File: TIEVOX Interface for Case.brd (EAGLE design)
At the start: 67.5 x 70 mm, 27 parts, among them IC1 DMMT5401, IC2 DMMT5401, U1 DMP2305U-7, U2 DMP2305U-7, U4 CAT24C32.UDFN8

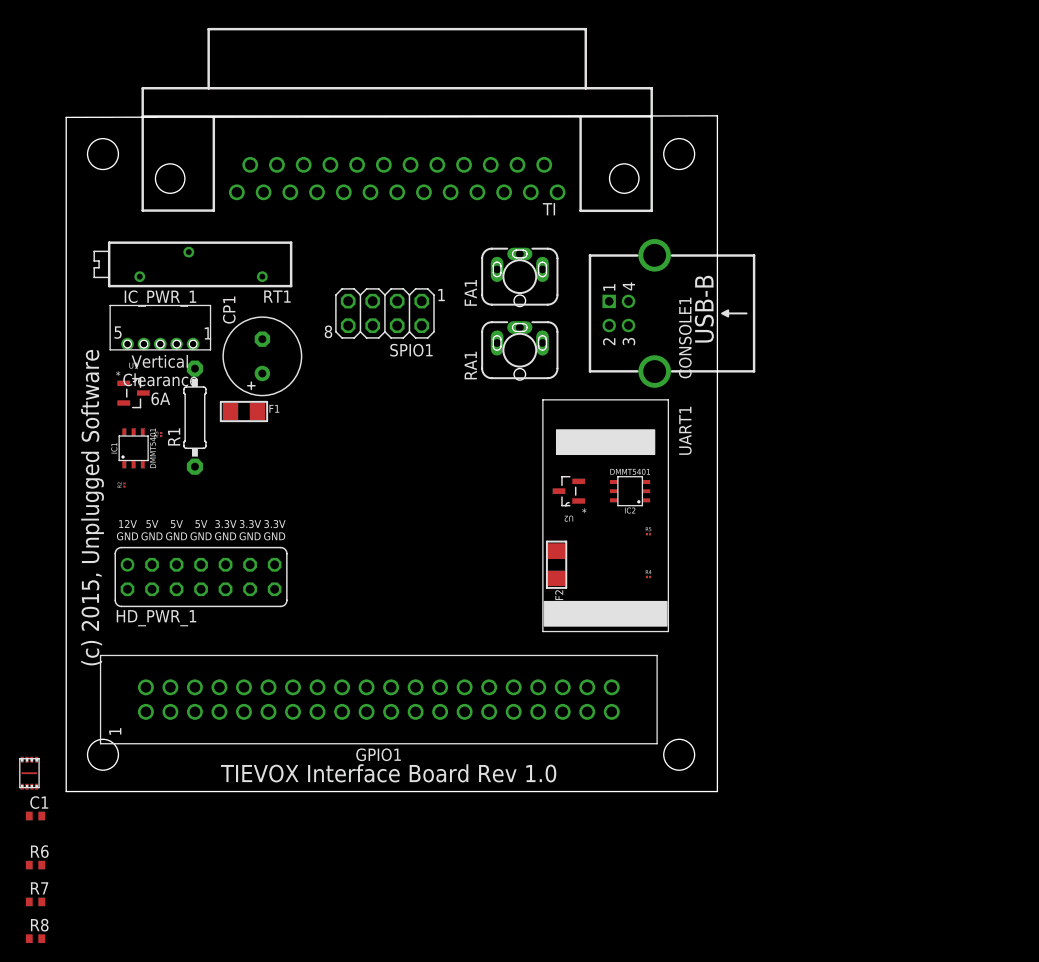
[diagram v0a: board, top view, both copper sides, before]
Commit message: Split TIEVOX Interface into two separate boards, a HAT and a version for the case I will be using that does not satisfy all the HAT requirements.
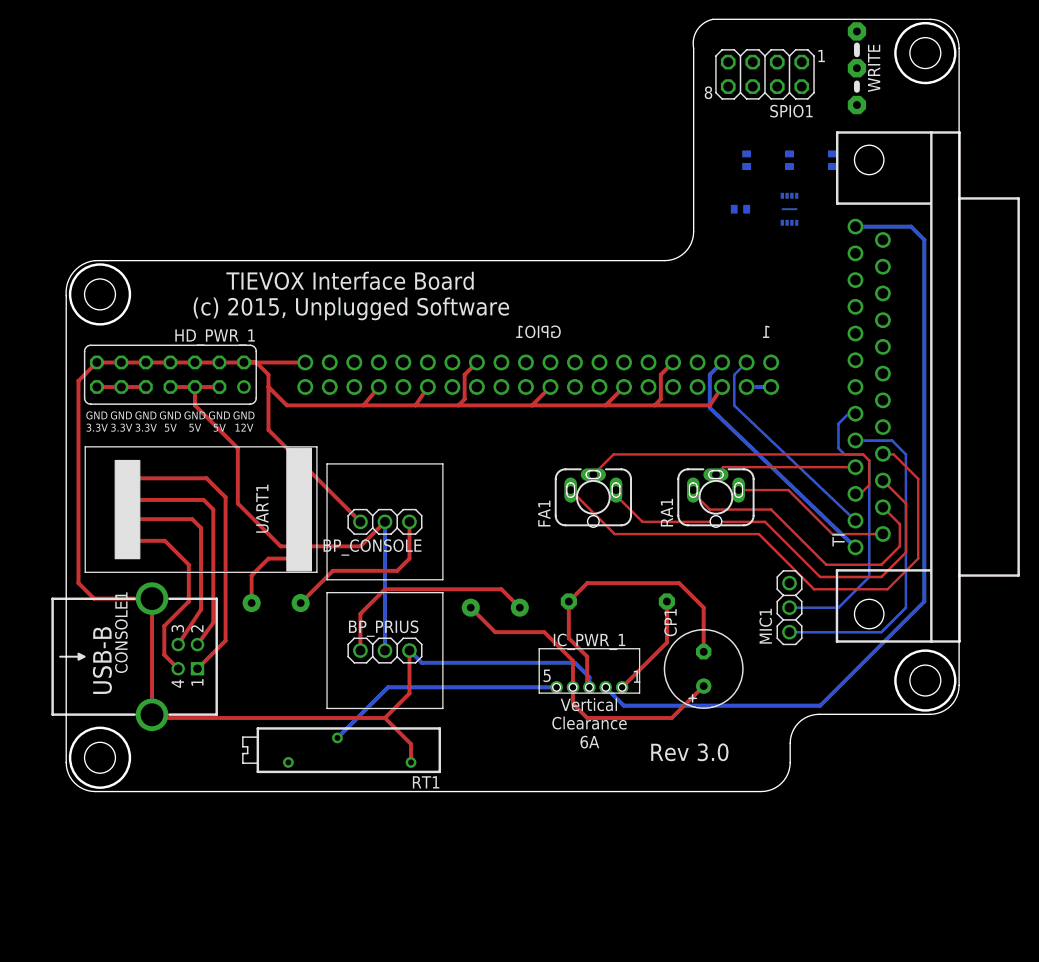
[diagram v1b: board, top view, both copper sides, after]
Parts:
- removed IC1, IC2: DMMT5401, Diodes_Inc_By_element14_Batch_1:DMMT5401
- removed R2, R4: 10K,1%, rcl:R01005
- removed R3, R5: 47K,1%, rcl:R01005
- removed U1, U2: DMP2305U-7, Diodes_Inc_By_element14_Batch_1:SOT103P240X110-3N
- added BP_CONSOLE, BP_PRIUS: BACKPOWER, connectors:BACKPOWER
- added MIC1: (no value), adafruit:1X03
- added WRITE: (no value), jumper:04C
- F1, F2: value PT1206L -> 06R155BPR; device microbuilder:1206 -> SparkFun-PowerIC:PTC
- GPIO1: value RPI_GPIOUPPER -> RPI_GPIO_FEMALE_LOWER; device connectors:RPI_GPIO_MALE -> connectors:RPI_GPIO_FEMALE_BOTTOM
- moved R8 115.4 mm to (79.4, 65.4), flipped to the bottom, turned to 90 degrees
- moved R6 106.9 mm to (74.9, 65.4), flipped to the bottom, turned to 90 degrees
- moved R7 106.4 mm to (70.5, 65.4), flipped to the bottom, turned to 90 degrees
- moved U4 98.0 mm to (74.9, 60.3), flipped to the bottom, turned to 180 degrees
- moved C1 96.4 mm to (69.8, 60.3), flipped to the bottom, turned to 180 degrees
- moved CONSOLE1 63.1 mm to (8.89, 14.0), turned to 90 degrees
- moved IC_PWR_1 56.9 mm to (50.8, 10.8)
- moved CP1 56.0 mm to (66.0, 12.7)
- moved TI 53.4 mm to (83.2, 41.9), turned to 90 degrees
- moved RT1 52.6 mm to (28.1, 4.29)
- moved R1 47.8 mm to (57.1, 19.7), flipped to the bottom, turned to 180 degrees
- moved SPIO1 46.5 mm to (72.4, 74.3)
- moved UART1 41.9 mm to (14.0, 29.2), turned to 270 degrees
- moved GPIO1 37.5 mm to (48.9, 43.2), turned to 270 degrees
- moved F1 33.0 mm to (44.5, 19.1), flipped to the bottom, turned to 180 degrees
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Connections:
- removed net N$32: F2.1, IC2.E1, U2.3
- removed net N$33: IC1.C2, R3.2
- removed net N$34: IC2.C2, R5.2, U2.1
- removed net N$35: IC2.B1, IC2.B2, IC2.C1, R4.2
- new net N$37: MIC1.2, TI.8
- new net N$41: GPIO1.33_GPIO13, MIC1.3
- net +5VDC: now also BP_CONSOLE.PWR_OUT, BP_PRIUS.PWR_OUT; no longer IC1.E2, IC2.E2, U1.2, U2.2
- net 5VDC: now also F2.P$1; no longer F2.2
- net GND: now also BP_CONSOLE.GND, BP_PRIUS.GND, RT1.1, WRITE.3; no longer R2.1, R3.1, R4.1, R5.1, RT1.3
- net N$22: now also RA1.2; no longer RA1.3
- net N$23: now also RA1.3; no longer RA1.2
- net N$28: now also F1.P$1; no longer F1.2
- net N$30: now also BP_PRIUS.PWR_IN, F1.P$2; no longer F1.1, IC1.E1, U1.3
- net N$31: now also BP_CONSOLE.PWR_IN, F2.P$2; no longer IC1.B1, IC1.B2, IC1.C1, R2.2
- net N$36: now also MIC1.1, TI.9; no longer U1.1
- net N$39: now also WRITE.2
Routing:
- net GND: track 0.00 -> 246.2 mm
- net PWR12_IN: track 0.00 -> 83.5 mm
- net N$25: track 0.00 -> 54.6 mm
- net +5VDC: track 0.00 -> 53.0 mm
- net N$24: track 0.00 -> 43.6 mm
- net N$36: track 0.00 -> 34.8 mm
- net N$20: track 0.00 -> 34.0 mm
- net N$28: track 0.00 -> 32.8 mm
- net N$22: track 0.00 -> 30.3 mm
- net N$37: track 0.00 -> 30.1 mm
- net N$15: track 0.00 -> 29.9 mm
- net N$27: track 0.00 -> 26.1 mm
- net PWR12_TRIM: track 0.00 -> 24.9 mm
- net N$16: track 0.00 -> 23.8 mm
- net N$26: track 0.00 -> 22.3 mm
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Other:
- board size 67.5 x 70 mm -> 92.5 x 80 mm
- board text added: "Rev 3.0"
- board text added: "TIEVOX Interface Board (c) 2015, Unplugged Software"
- board text removed: "(c) 2015, Unplugged Software"
- board text removed: "TIEVOX Interface Board Rev 1.0"

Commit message: Added LICENSE.md.
Exported library for GPIO Protect & Split.
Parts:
- moved HD_PWR_1 43.6 mm to (52.1, 29.2), turned to 0 degrees
- moved SPIO1 21.0 mm to (72.4, 53.3), turned to 0 degrees
- moved FA1 16.1 mm to (69.8, 35.6)
- moved GPIO1 10.8 mm to (38.1, 43.8)
- moved R6 8.98 mm to (73.7, 74.3)
- moved U4 8.98 mm to (73.7, 69.2)
- moved C1 8.98 mm to (68.6, 69.2)
- moved R7 8.98 mm to (69.2, 74.3)
- moved R8 8.98 mm to (78.1, 74.3)
- moved WRITE 8.13 mm to (88.3, 71.8), turned to 180 degrees
- moved RA1 3.59 mm to (69.8, 27.9)
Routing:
- net GND: track 246.2 -> 0.00 mm
- net PWR12_IN: track 83.5 -> 0.00 mm
- net N$25: track 54.6 -> 0.00 mm
- net +5VDC: track 53.0 -> 0.00 mm
- net N$24: track 43.6 -> 0.00 mm
- net N$36: track 34.8 -> 0.00 mm
- net N$20: track 34.0 -> 0.00 mm
- net N$28: track 32.8 -> 0.00 mm
- net N$22: track 30.3 -> 0.00 mm
- net N$37: track 30.1 -> 0.00 mm
- net N$15: track 29.9 -> 0.00 mm
- net N$27: track 26.1 -> 0.00 mm
- net PWR12_TRIM: track 24.9 -> 0.00 mm
- net N$16: track 23.8 -> 0.00 mm
- net N$26: track 22.3 -> 0.00 mm
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
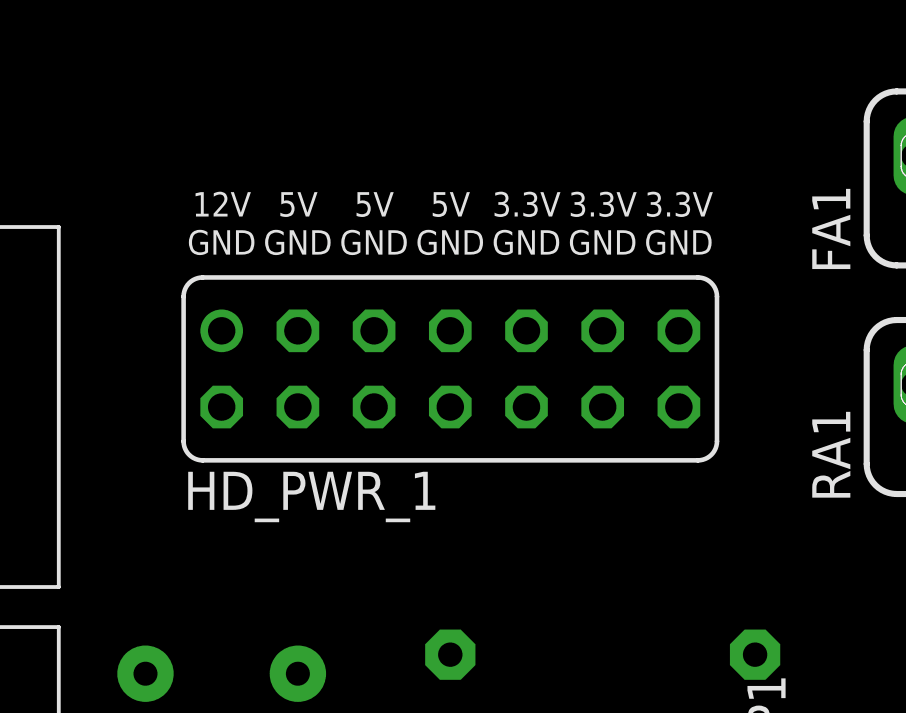
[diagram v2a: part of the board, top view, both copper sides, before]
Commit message: Removed power header. Not sure that it's needed, and need to see if that'll help get everything routed.
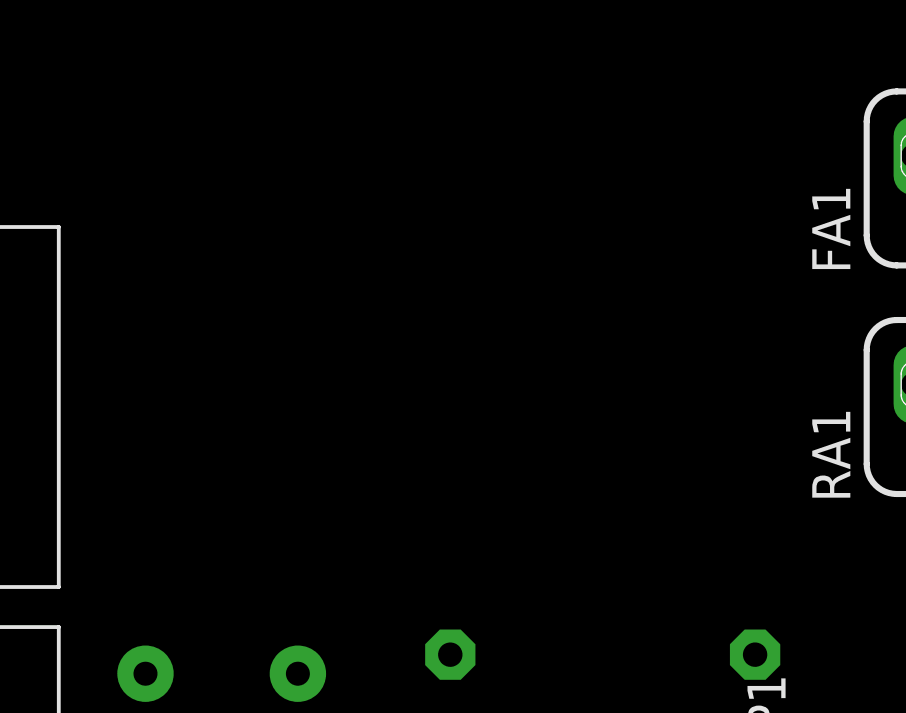
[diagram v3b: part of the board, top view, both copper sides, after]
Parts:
- removed HD_PWR_1: PWR_HDR_FEMALE_2X7, con-lsta:PWR_HDR_FEMALE_2X7
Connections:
- net +3.3VDC: no longer HD_PWR_1.+3.3VDC1, HD_PWR_1.+3.3VDC2, HD_PWR_1.+3.3VDC3
- net +5VDC: no longer HD_PWR_1.+5VDC1, HD_PWR_1.+5VDC2, HD_PWR_1.+5VDC3
- net GND: no longer HD_PWR_1.GND1, HD_PWR_1.GND2, HD_PWR_1.GND3, HD_PWR_1.GND4, HD_PWR_1.GND5, HD_PWR_1.GND6, HD_PWR_1.GND7
- net PWR12_IN: no longer HD_PWR_1.+12VDC
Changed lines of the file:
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@@
 <element name="CP1" library="rcl" package="E3,5-8" value="1000uF" x="66.04" y="12.7" rot="R90"/>
 <element name="GPIO1" library="connectors" package="RPI_GPIO_FEMALE_BOTTOM" value="RPI_GPIO_FEMALE_LOWER" x="38.1" y="43.815" rot="R270"/>
-<element name="HD_PWR_1" library="con-lsta" package="PWR_HDR_FEMALE_2X7" value="PWR_HDR_FEMALE_2X7" x="52.07" y="29.21"/>
 <element name="IC_PWR_1" library="packages" package="NE12S" value="6A" x="50.8" y="10.795"/>
 <element name="SPIO1" library="pinhead" package="2X04" value="2.4GHz" x="72.39" y="53.34"/>
@@
 <contactref element="GPIO1" pad="4_5VDC"/>
 <contactref element="TI" pad="5"/>
-<contactref element="HD_PWR_1" pad="+5VDC1"/>
-<contactref element="HD_PWR_1" pad="+5VDC2"/>
-<contactref element="HD_PWR_1" pad="+5VDC3"/>
 <contactref element="BP_PRIUS" pad="PWR_OUT"/>
 <contactref element="BP_CONSOLE" pad="PWR_OUT"/>
 <wire x1="62.23" y1="42.545" x2="81.7626" y2="47.4472" width="0" layer="19" extent="1-1"/>
 <wire x1="59.69" y1="42.545" x2="62.23" y2="42.545" width="0" layer="19" extent="1-1"/>
-<wire x1="52.07" y1="30.48" x2="59.69" y2="42.545" width="0" layer="19" extent="1-1"/>
-<wire x1="49.53" y1="30.48" x2="52.07" y2="30.48" width="0" layer="19" extent="1-1"/>
-<wire x1="46.99" y1="30.48" x2="49.53" y2="30.48" width="0" layer="19" extent="1-1"/>
-<wire x1="33.02" y1="27.94" x2="46.99" y2="30.48" width="0" layer="19" extent="1-1"/>
+<wire x1="33.02" y1="27.94" x2="59.69" y2="42.545" width="0" layer="19" extent="1-1"/>
 <wire x1="33.02" y1="14.605" x2="33.02" y2="27.94" width="0" layer="19" extent="1-1"/>
 </signal>
@@
 <contactref element="CONSOLE1" pad="CASE2"/>
 <contactref element="CONSOLE1" pad="CASE1"/>
-<contactref element="HD_PWR_1" pad="GND1"/>
-<contactref element="HD_PWR_1" pad="GND2"/>
-<contactref element="HD_PWR_1" pad="GND3"/>
-<contactref element="HD_PWR_1" pad="GND4"/>
-<contactref element="HD_PWR_1" pad="GND5"/>
-<contactref element="HD_PWR_1" pad="GND6"/>
-<contactref element="HD_PWR_1" pad="GND7"/>
 <contactref element="CP1" pad="-"/>
 <contactref element="R1" pad="1"/>
@@
 <wire x1="24.13" y1="34.29" x2="26.67" y2="42.545" width="0" layer="19" extent="1-1"/>
 <wire x1="30.48" y1="27.94" x2="24.13" y2="34.29" width="0" layer="19" extent="1-1"/>
-<wire x1="44.45" y1="27.94" x2="30.48" y2="27.94" width="0" layer="19" extent="1-1"/>
-<wire x1="46.99" y1="27.94" x2="44.45" y2="27.94" width="0" layer="19" extent="1-1"/>
-<wire x1="49.53" y1="27.94" x2="46.99" y2="27.94" width="0" layer="19" extent="1-1"/>
-<wire x1="52.07" y1="27.94" x2="49.53" y2="27.94" width="0" layer="19" extent="1-1"/>
-<wire x1="54.61" y1="27.94" x2="52.07" y2="27.94" width="0" layer="19" extent="1-1"/>
-<wire x1="57.15" y1="27.94" x2="54.61" y2="27.94" width="0" layer="19" extent="1-1"/>
-<wire x1="59.69" y1="27.94" x2="57.15" y2="27.94" width="0" layer="19" extent="1-1"/>
-<wire x1="52.07" y1="19.685" x2="52.07" y2="27.94" width="0" layer="19" extent="1-1"/>
+<wire x1="35.56" y1="14.605" x2="30.48" y2="27.94" width="0" layer="19" extent="1-1"/>
+<wire x1="35.71875" y1="3.01625" x2="35.56" y2="14.605" width="0" layer="19" extent="1-1"/>
+<wire x1="52.07" y1="19.685" x2="35.56" y2="14.605" width="0" layer="19" extent="1-1"/>
 <wire x1="54.2" y1="10.795" x2="52.07" y2="19.685" width="0" layer="19" extent="1-1"/>
 <wire x1="66.04" y1="14.478" x2="54.2" y2="10.795" width="0" layer="19" extent="1-1"/>
-<wire x1="35.56" y1="14.605" x2="30.48" y2="27.94" width="0" layer="19" extent="1-1"/>
-<wire x1="35.71875" y1="3.01625" x2="35.56" y2="14.605" width="0" layer="19" extent="1-1"/>
 <wire x1="8.89" y1="19.99" x2="24.13" y2="34.29" width="0" layer="19" extent="1-1"/>
 <wire x1="8.89" y1="7.95" x2="8.89" y2="19.99" width="0" layer="19" extent="1-1"/>
@@
 <contactref element="TI" pad="4"/>
 <contactref element="SPIO1" pad="2"/>
-<contactref element="HD_PWR_1" pad="+3.3VDC1"/>
-<contactref element="HD_PWR_1" pad="+3.3VDC2"/>
-<contactref element="HD_PWR_1" pad="+3.3VDC3"/>
 <contactref element="C1" pad="2"/>
 <contactref element="U4" pad="8"/>
@@
 <wire x1="62.23" y1="45.085" x2="68.58" y2="54.61" width="0" layer="19" extent="1-1"/>
 <wire x1="81.7626" y1="50.2158" x2="68.58" y2="54.61" width="0" layer="19" extent="1-1"/>
-<wire x1="59.69" y1="30.48" x2="62.23" y2="45.085" width="0" layer="19" extent="1-1"/>
-<wire x1="57.15" y1="30.48" x2="59.69" y2="30.48" width="0" layer="19" extent="1-1"/>
-<wire x1="54.61" y1="30.48" x2="57.15" y2="30.48" width="0" layer="19" extent="1-1"/>
-<wire x1="41.91" y1="45.085" x2="54.61" y2="30.48" width="0" layer="19" extent="1-1"/>
+<wire x1="41.91" y1="45.085" x2="62.23" y2="45.085" width="0" layer="19" extent="1-1"/>
 </signal>
 <signal name="PWR12_TRIM">
@@
 <contactref element="TI" pad="1"/>
 <contactref element="IC_PWR_1" pad="VIN"/>
-<contactref element="HD_PWR_1" pad="+12VDC"/>
-<wire x1="44.45" y1="30.48" x2="81.7626" y2="58.5216" width="0" layer="19" extent="1-1"/>
-<wire x1="55.88" y1="10.795" x2="44.45" y2="30.48" width="0" layer="19" extent="1-1"/>
+<wire x1="55.88" y1="10.795" x2="81.7626" y2="58.5216" width="0" layer="19" extent="1-1"/>
 </signal>
 <signal name="N$1">

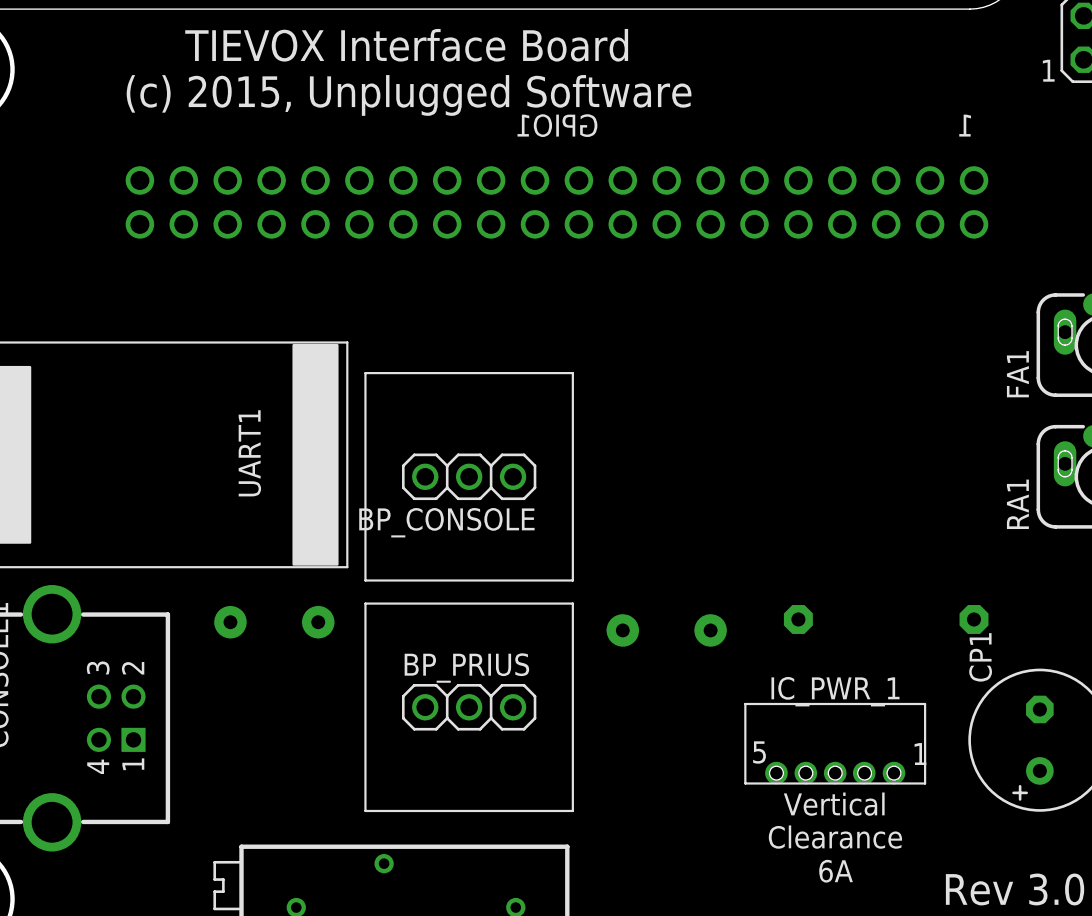
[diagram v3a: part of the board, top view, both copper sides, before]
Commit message: Removed extraneous ground and +VDC connections to GPIO to aid in routing.
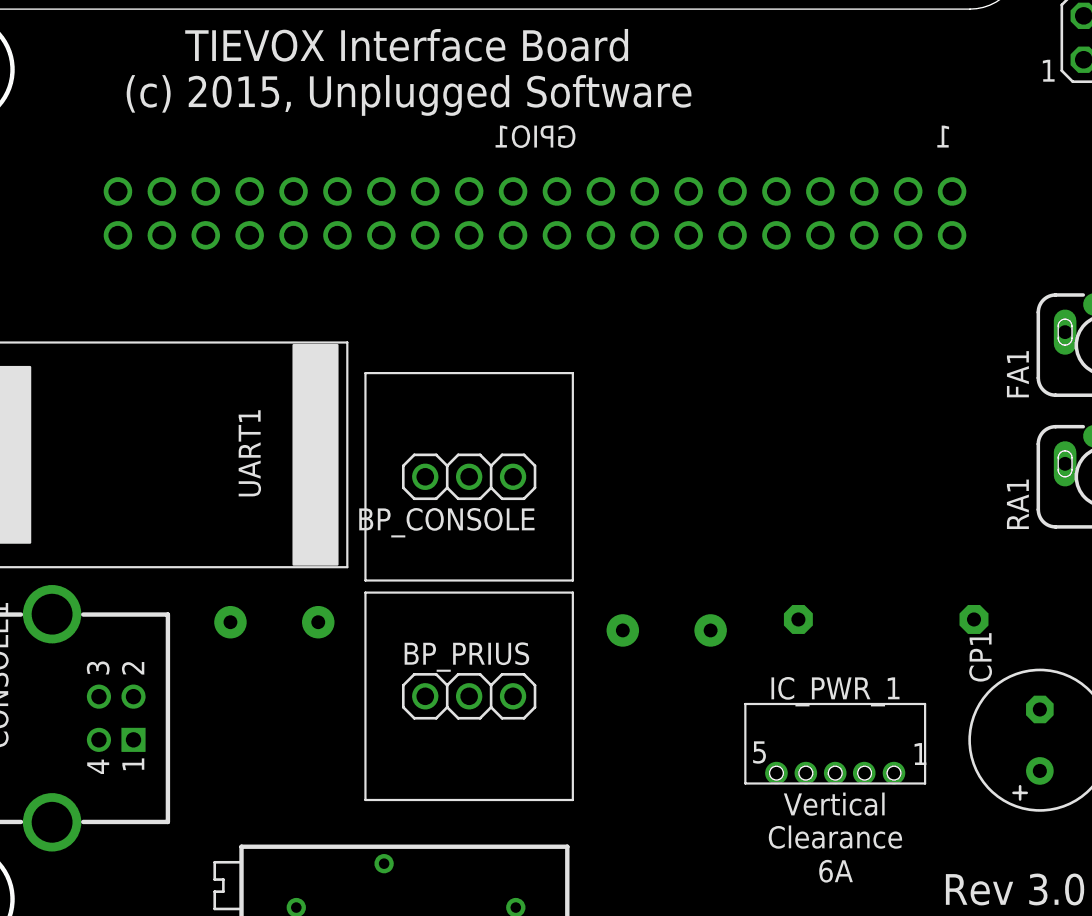
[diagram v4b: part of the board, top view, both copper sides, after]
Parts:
- moved GPIO1 1.42 mm to (36.8, 43.2)
- moved BP_PRIUS 0.63 mm to (33.0, 15.2)
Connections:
- new net 17_3.3VDC: GPIO1.17_3.3VDC
- new net 20_GND: GPIO1.20_GND
- new net 25_GND: GPIO1.25_GND
- new net 30_GND: GPIO1.30_GND
- new net 34_GND: GPIO1.34_GND
- new net 39_GND: GPIO1.39_GND
- new net 4_5VDC: GPIO1.4_5VDC
- new net 9_GND: GPIO1.9_GND
- net +3.3VDC: no longer GPIO1.17_3.3VDC
- net +5VDC: no longer GPIO1.4_5VDC
- net GND: no longer GPIO1.20_GND, GPIO1.25_GND, GPIO1.30_GND, GPIO1.34_GND, GPIO1.39_GND, GPIO1.9_GND
